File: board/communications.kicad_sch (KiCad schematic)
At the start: 9 parts, among them J1 RJ45_LED_Shielded, U3 ATA6561

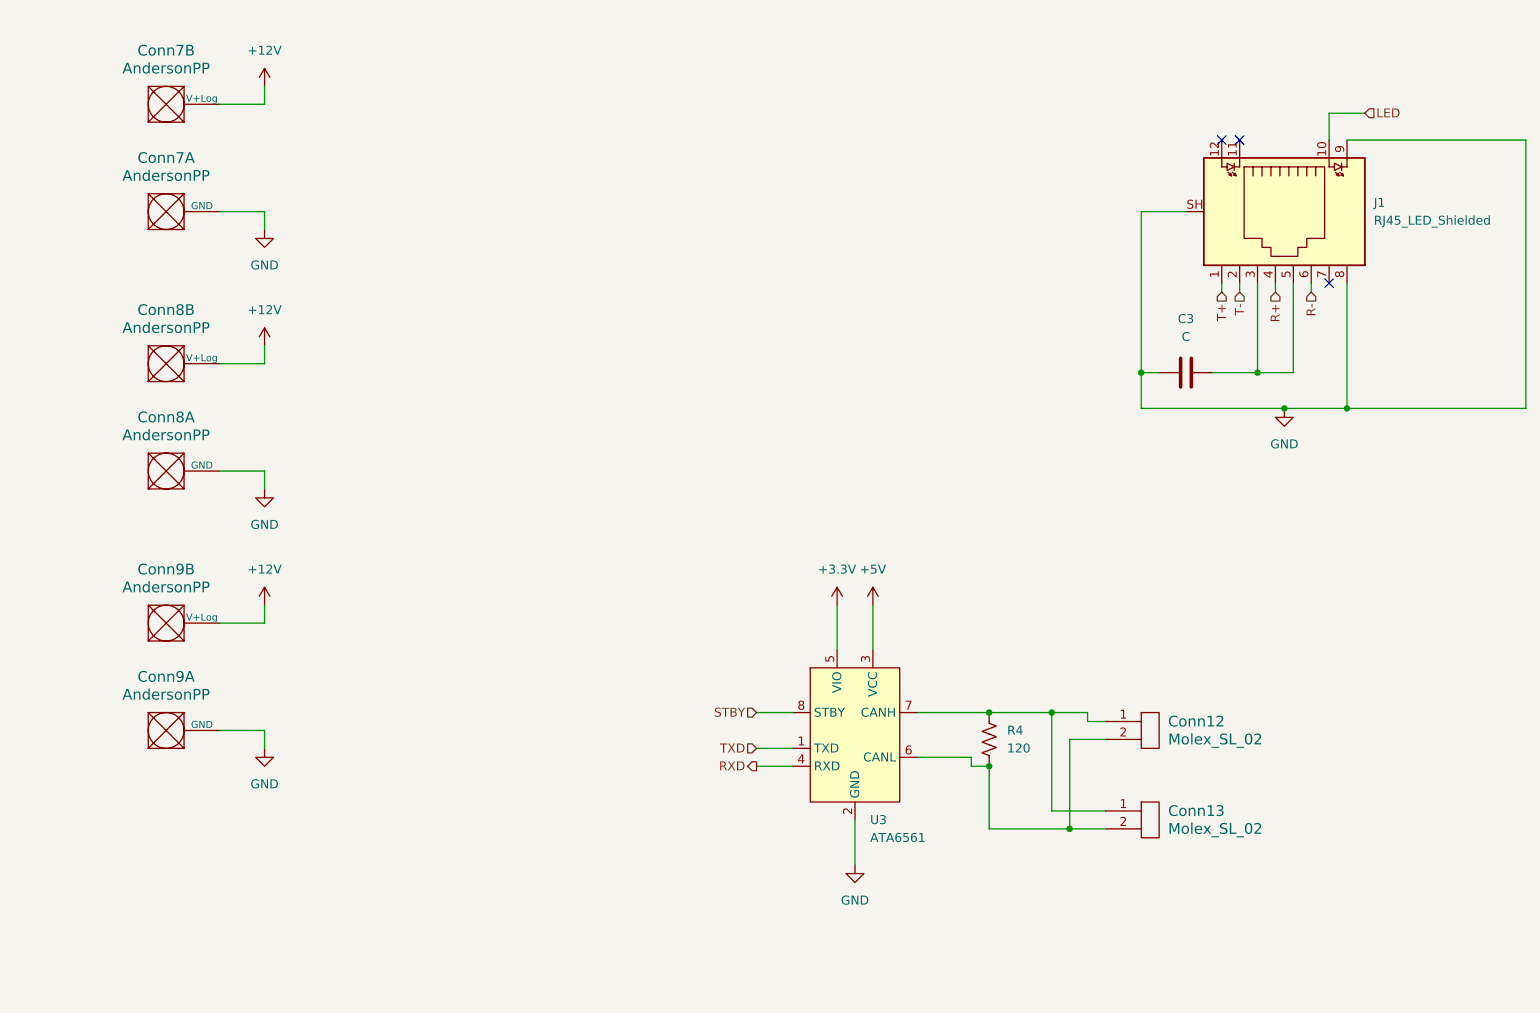
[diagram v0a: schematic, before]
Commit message: Added Servo, cleaned up schematic
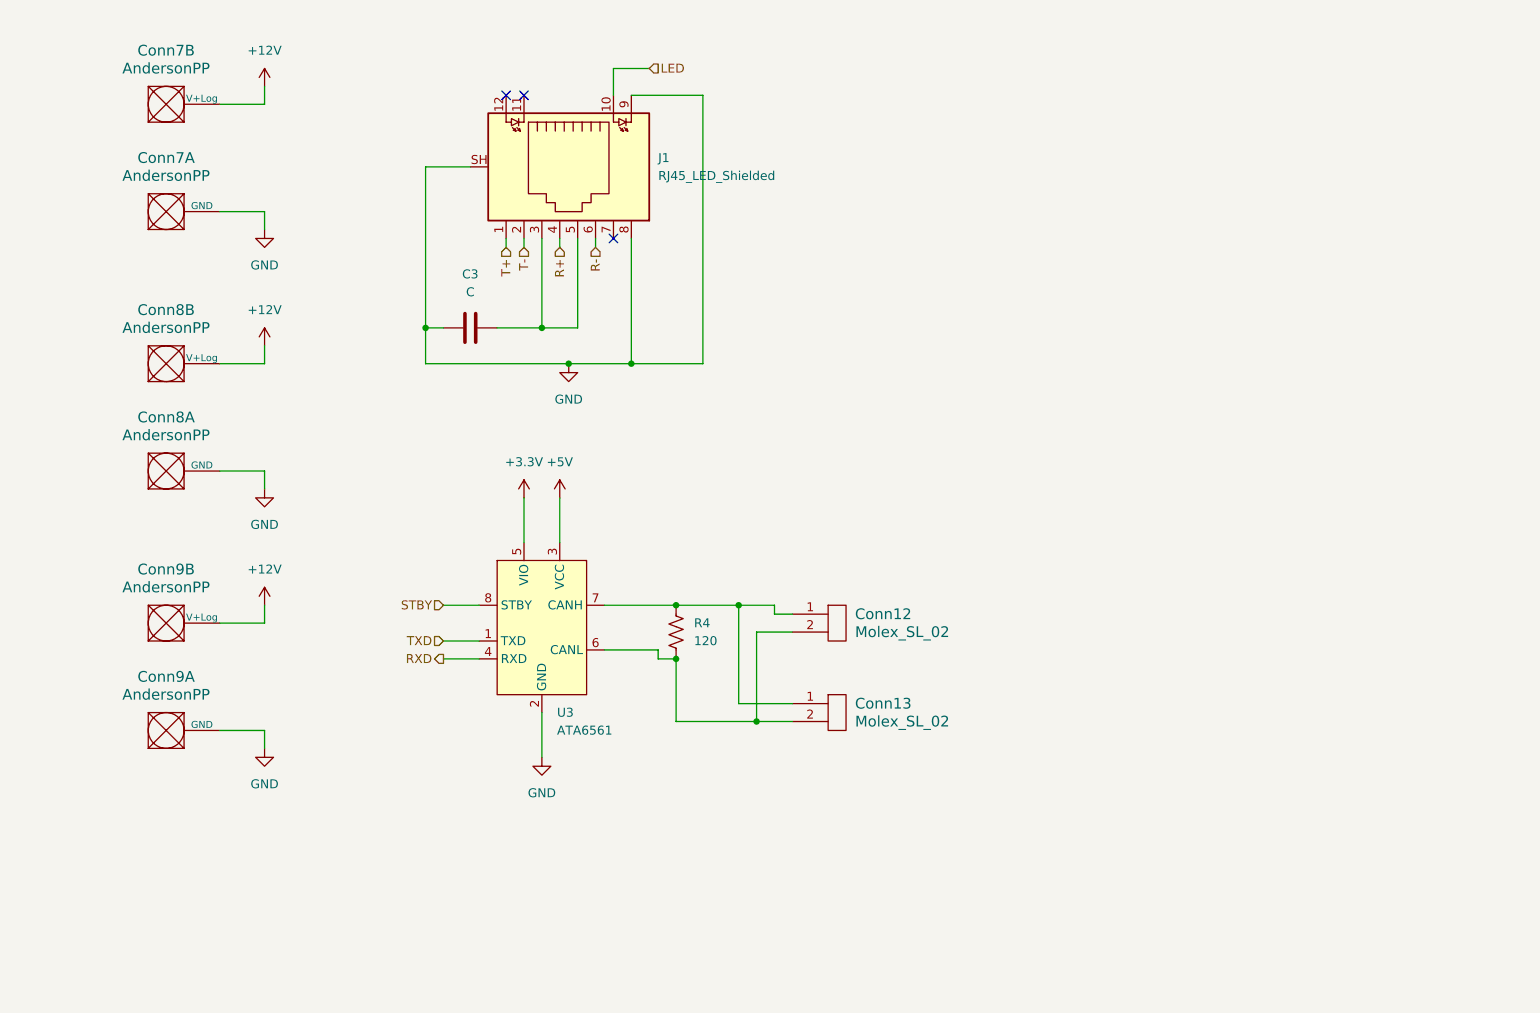
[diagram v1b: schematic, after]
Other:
- moved on the sheet: C3, Conn12, Conn13, J1, R4, U3

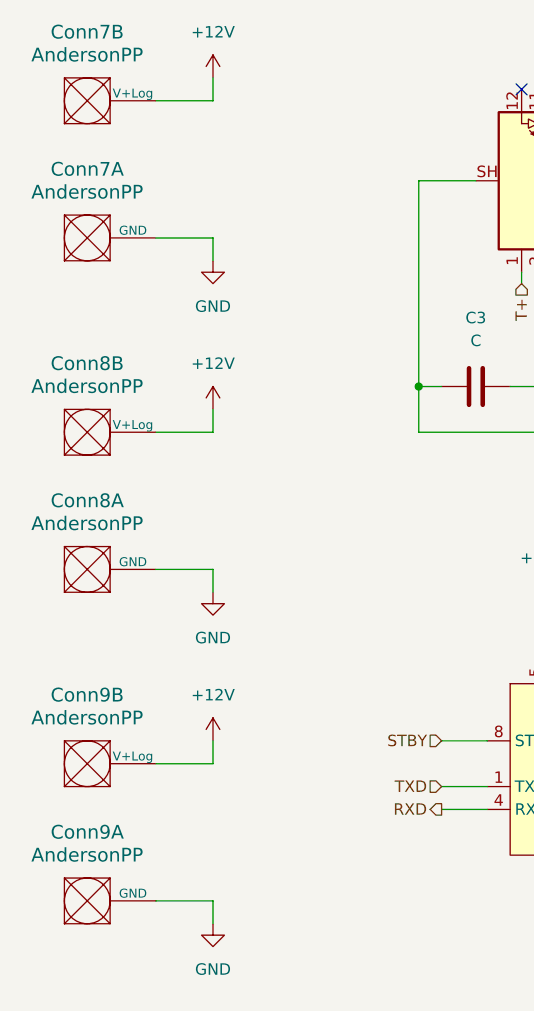
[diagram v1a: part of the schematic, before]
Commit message: Moved things to make more sense
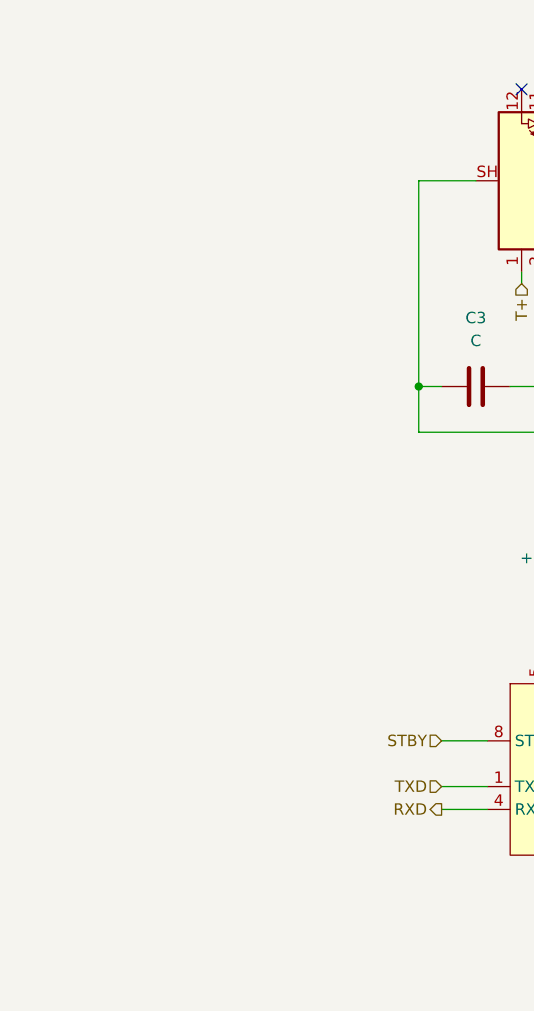
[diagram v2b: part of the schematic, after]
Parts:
- removed Conn7, Conn8, Conn9: AndersonPP, symbol MRDT_Connectors:AndersonPP

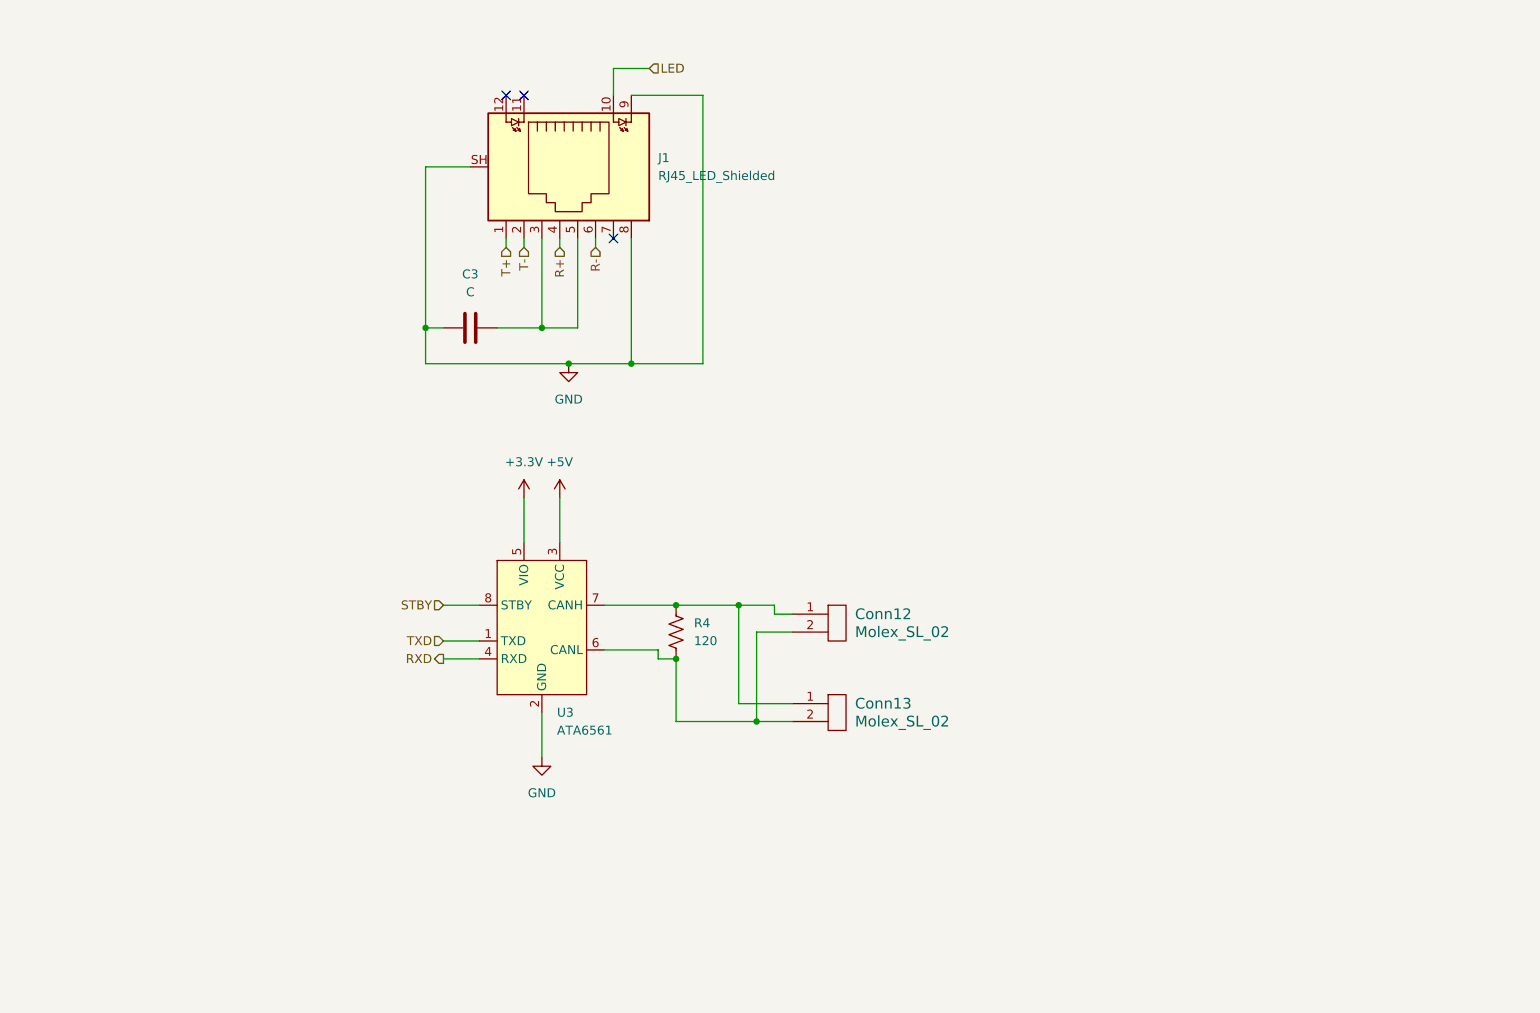
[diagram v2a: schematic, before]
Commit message: Added Labels, Missing Requirements, and Refined Look
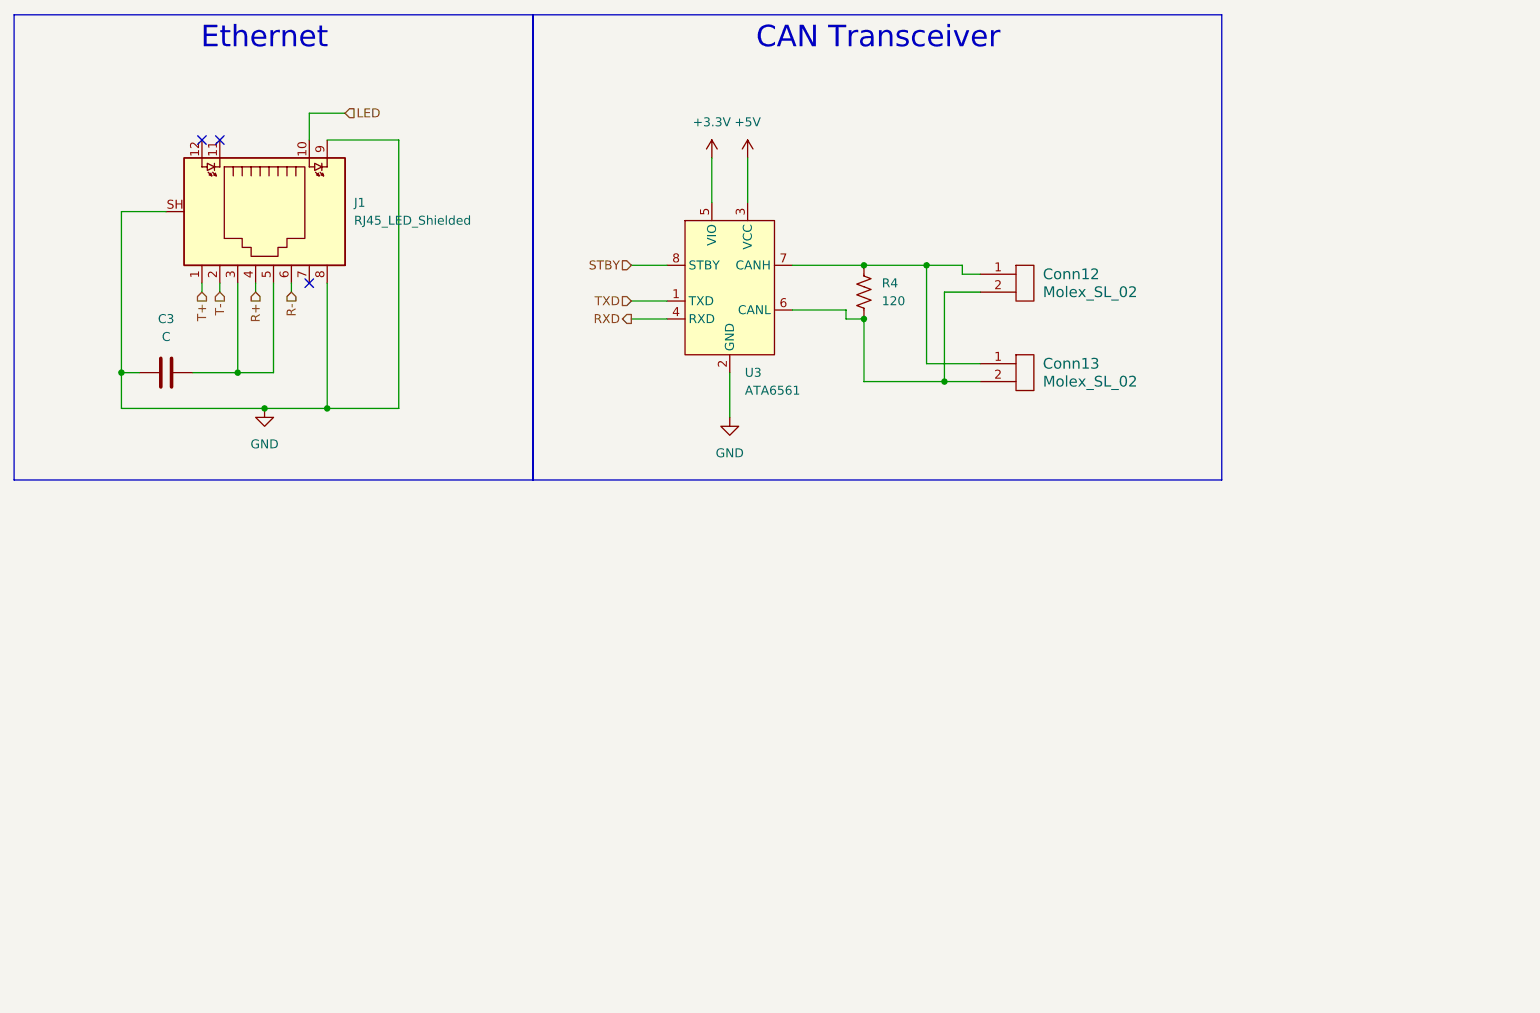
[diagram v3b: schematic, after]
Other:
- note added: "CAN Transceiver"
- note added: "Ethernet"
- moved on the sheet: C3, Conn12, Conn13, J1, R4, U3

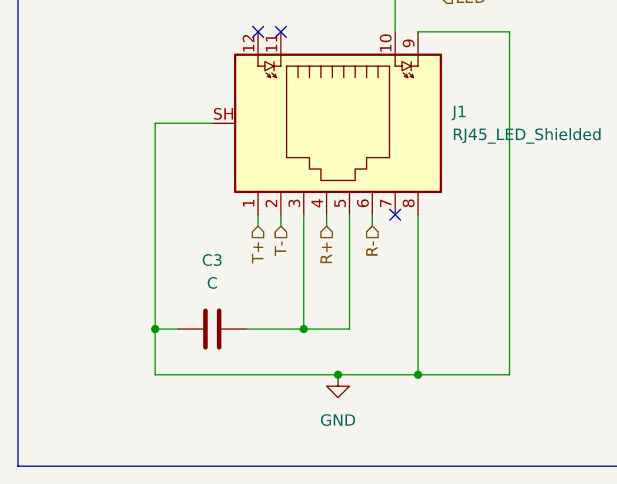
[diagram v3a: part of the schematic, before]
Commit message: assigned footprints
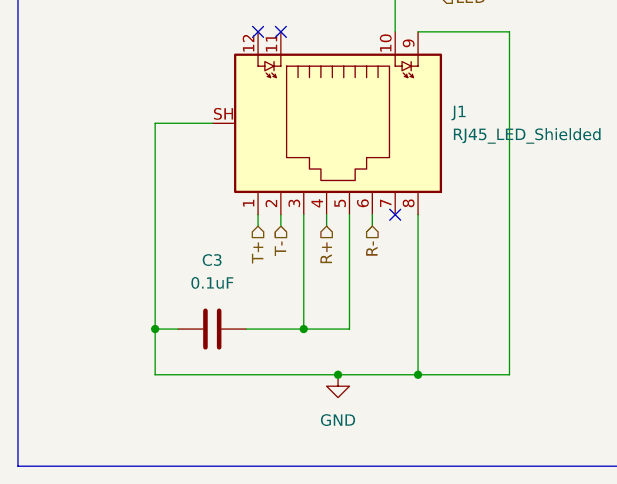
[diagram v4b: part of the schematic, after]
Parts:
- C3: value C -> 0.1uF; footprint (none) -> Capacitor_SMD:C_0603_1608Metric_Pad1.08x0.95mm_HandSolder
- Conn12, Conn13: footprint (none) -> MRDT_Connectors:MOLEX_SL_02_Vertical
- J1: footprint (none) -> MRDT_Connectors:RJ45_Teensy
- R4: footprint (none) -> Resistor_SMD:R_0603_1608Metric_Pad0.98x0.95mm_HandSolder
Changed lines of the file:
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@@
 			)
 		)
-		(property "Footprint" ""
+		(property "Footprint" "MRDT_Connectors:MOLEX_SL_02_Vertical"
 			(at 154.94 55.88 0)
 			(effects
@@
 			)
 		)
-		(property "Footprint" ""
+		(property "Footprint" "Resistor_SMD:R_0603_1608Metric_Pad0.98x0.95mm_HandSolder"
 			(at 134.366 52.324 90)
 			(effects
@@
 			)
 		)
-		(property "Footprint" ""
+		(property "Footprint" "MRDT_Connectors:RJ45_Teensy"
 			(at 47.625 40.64 90)
 			(effects
@@
 			)
 		)
-		(property "Footprint" ""
+		(property "Footprint" "MRDT_Connectors:MOLEX_SL_02_Vertical"
 			(at 154.94 68.58 0)
 			(effects
@@
 			)
 		)
-		(property "Value" "C"
+		(property "Value" "0.1uF"
 			(at 34.29 58.42 90)
 			(effects
@@
 			)
 		)
-		(property "Footprint" ""
+		(property "Footprint" "Capacitor_SMD:C_0603_1608Metric_Pad1.08x0.95mm_HandSolder"
 			(at 38.1 62.5348 0)
 			(effects
